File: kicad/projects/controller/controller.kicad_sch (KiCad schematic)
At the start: 30 parts, among them J1 Buttons, J2 Joystick1, J3 Joystick2, J4 Display, J5 18650, J6 Rumble1, J7 Rumble2, J8 ADS1115, Q1 DMG2301L, Q2 MMBT2222A, SW2 SW_DP3T, U2 ESP32-C6-SUPERMINI, U3 MCP1826T-3302E/DC

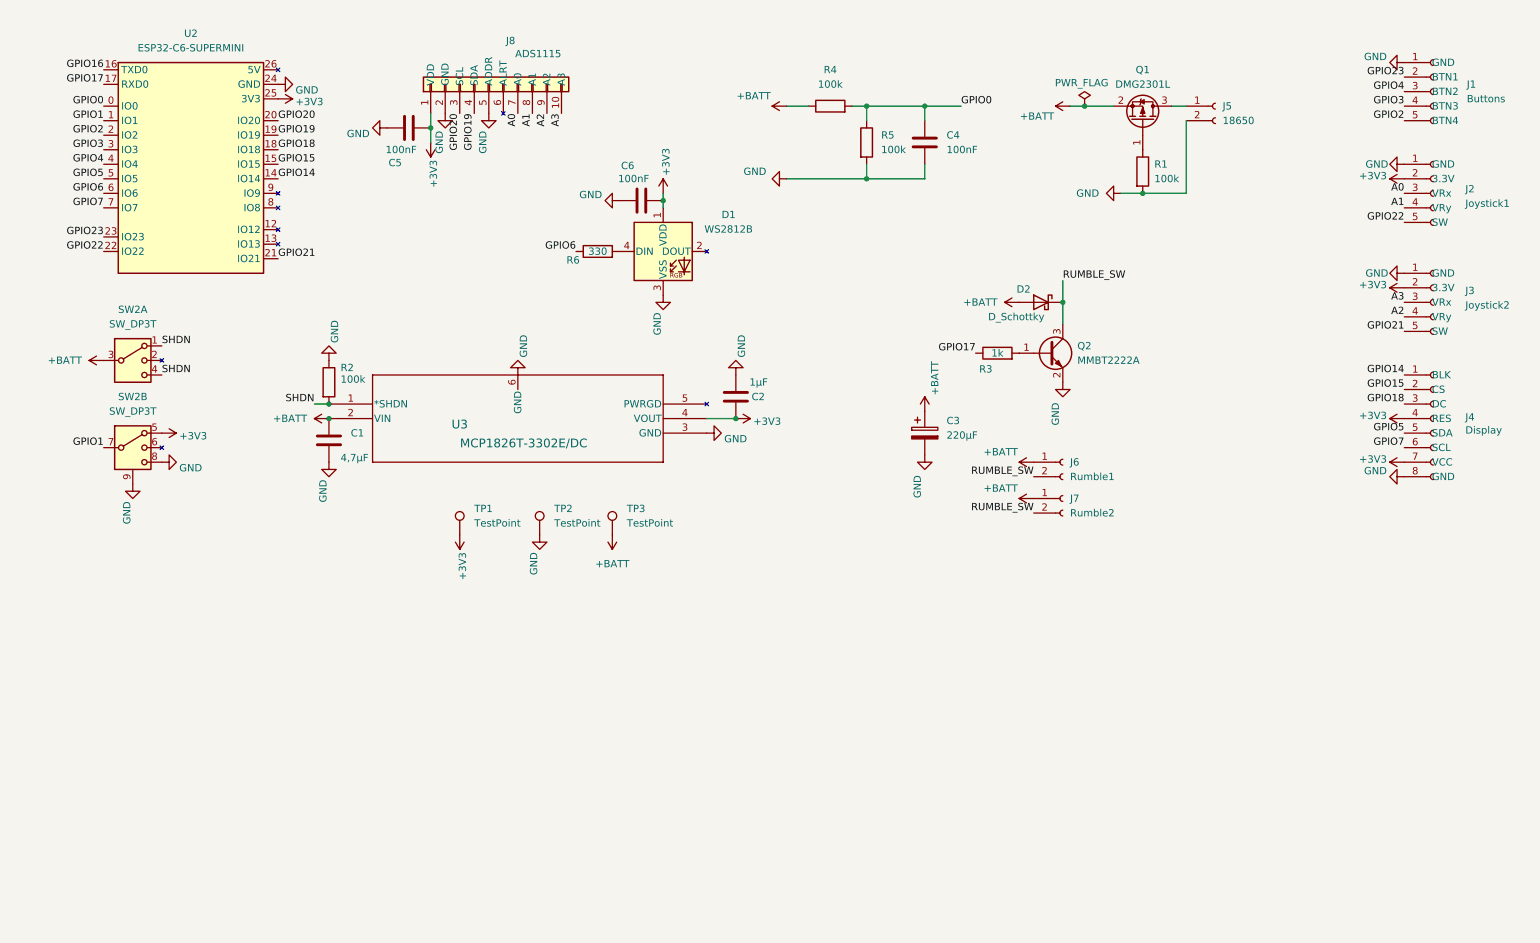
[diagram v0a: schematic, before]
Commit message: Repo für Veröffentlichung vorbereitet: KiCad-Struktur, Lizenz, Aufräumen
- KiCad-Projekte je Platine nach kicad/projects/<board>/ (kart, controller,
  buttons, switch), eigene Bibliotheken nach kicad/libs/, projektlokale
  sym-lib-table/fp-lib-table auf ${KIPRJMOD}/../../libs
- Schalter-Platinchen: einschalter -> switch, Titelblock vereinheitlicht
- AO4407A: 3D-Modell auf KiCad-Standard-SOIC-8, Footprint-Verweis korrigiert
- Alte Stände nach kicad/archive/ (FB-V1-Layout, D1-Mini-Schaltplan)
- Lizenz CC BY-NC-SA 4.0, Fan-Projekt-Hinweis
- CLAUDE.md nicht mehr versioniert, PDFs/DOCX/Exporte ignoriert
- Laufende Firmware-Änderungen (Kart V2, FB V2, Stern-Licht) mitcommittet
- docs/wiki-plan.md: Arbeitsliste für das Wiki

Co-Authored-By: Claude Opus 5.5 <noreply@anthropic.com>
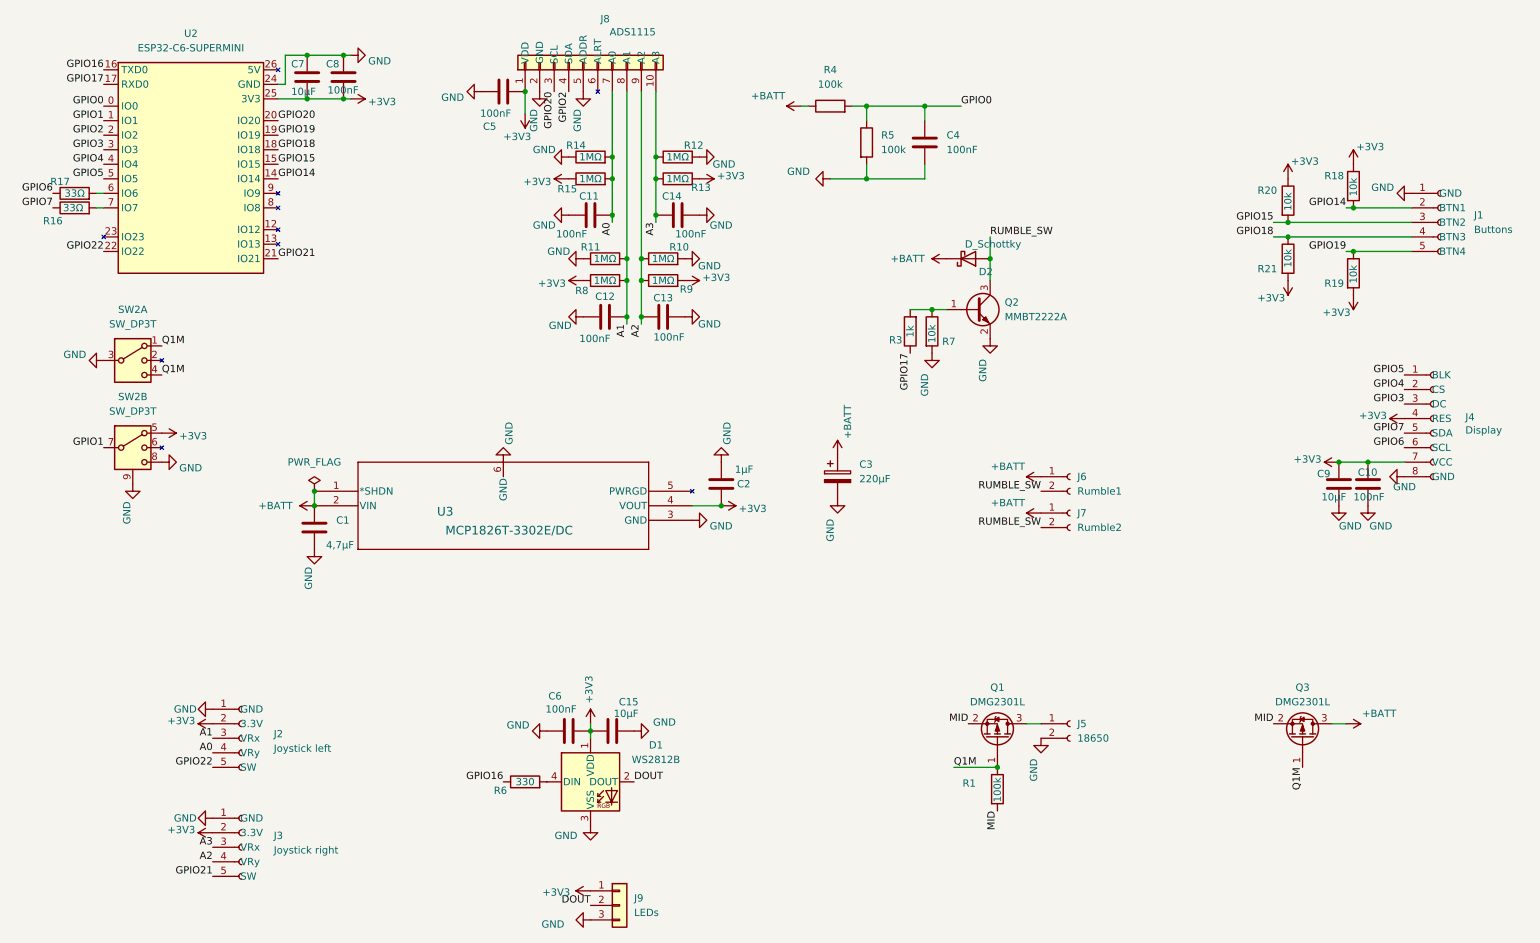
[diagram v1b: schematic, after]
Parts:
- removed R2: 100k, Resistor_SMD:R_0805_2012Metric_Pad1.20x1.40mm_HandSolder, symbol Device:R
- removed TP1, TP2, TP3: TestPoint, TestPoint:TestPoint_Pad_D2.0mm, symbol Connector:TestPoint
- added C10, C11, C12, C13, C14, C8: 100nF, Capacitor_SMD:C_0805_2012Metric_Pad1.18x1.45mm_HandSolder, symbol Device:C
- added C15, C7, C9: 10µF, Capacitor_SMD:C_1206_3216Metric_Pad1.33x1.80mm_HandSolder, symbol Device:C
- added J9: LEDs, Connector_PinHeader_2.54mm:PinHeader_1x03_P2.54mm_Vertical, symbol Connector_Generic:Conn_01x03
- added Q3: DMG2301L, Package_TO_SOT_SMD:SOT-23_Handsoldering, symbol Transistor_FET:DMG2301L
- added R10, R11, R12, R13, R14, R15, R8, R9: 1MΩ, Resistor_SMD:R_0805_2012Metric_Pad1.20x1.40mm_HandSolder, symbol Device:R
- added R16, R17: 33Ω, Resistor_SMD:R_0805_2012Metric_Pad1.20x1.40mm_HandSolder, symbol Device:R
- added R18, R19, R20, R21, R7: 10k, Resistor_SMD:R_0805_2012Metric_Pad1.20x1.40mm_HandSolder, symbol Device:R
- J1: footprint Connector_JST:JST_XH_S5B-XH-A-1_1x05_P2.50mm_Horizontal -> Connector_PinHeader_2.54mm:PinHeader_1x05_P2.54mm_Vertical
- J2: value Joystick1 -> Joystick left
- J3: value Joystick2 -> Joystick right
- J5: footprint Connector_Wire:SolderWire-1.5sqmm_1x02_P6mm_D1.7mm_OD3mm -> Connector_Wire:SolderWire-0.75sqmm_1x02_P4.8mm_D1.25mm_OD2.3mm
- J6, J7: footprint Connector_JST:JST_XH_S2B-XH-A-1_1x02_P2.50mm_Horizontal -> Connector_PinHeader_2.54mm:PinHeader_1x02_P2.54mm_Vertical
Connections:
- net +3V3: now also C10.1, C15.1, C7.2, C8.2, C9.1, J9.1 (Pin_1), R13.2, R15.1, R18.1, R19.2, R20.1, R21.2, R8.1, R9.2
- net +BATT: now also D2.1 (K), U3.1 (*SHDN), Q3.3 (D); no longer D2.2 (A), Q1.2 (S), SW2.3
- net A0: now also J2.4 (VRy), C11.2, R14.2, R15.2; no longer J2.3 (VRx)
- net A1: now also J2.3 (VRx), C12.1, R11.2, R8.2; no longer J2.4 (VRy)
- net A2: now also C13.1, R10.1, R9.1
- net A3: now also C14.1, R12.1, R13.1
- net GND: now also SW2.3, C10.2, C11.1, C12.2, C13.2, C14.2, C15.2, C7.1, C8.1, C9.2, J9.3 (Pin_3), R10.2, R11.1, R12.2, R14.1, R7.2; no longer R1.2
- net GPIO14: now also J1.2 (BTN1), R18.2; no longer J4.1 (BLK)
- net GPIO15: now also J1.3 (BTN2), R20.2; no longer J4.2 (CS)
- net GPIO16: now also R6.1
- net GPIO18: now also J1.4 (BTN3), R21.1; no longer J4.3 (DC)
- net GPIO19: now also J1.5 (BTN4), R19.1; no longer J8.4 (SDA)
- net GPIO2: now also J8.4 (SDA); no longer J1.5 (BTN4)
- net GPIO3: now also J4.3 (DC); no longer J1.4 (BTN3)
- net GPIO4: now also J4.2 (CS); no longer J1.3 (BTN2)
- net GPIO5: now also J4.1 (BLK); no longer J4.5 (SDA)
- net GPIO6: now also J4.6 (SCL), R17.1; no longer R6.1, U2.6 (IO6)
- net GPIO7: now also J4.5 (SDA), R16.1; no longer J4.6 (SCL), U2.7 (IO7)
- net RUMBLE_SW: now also D2.2 (A); no longer D2.1 (K)
- net Q1M: now reaches Q1.1 (G), R1.1
- net Q1M: now also SW2.1, SW2.4, Q3.1 (G)
- net at Q2.1 (B), R3.2: now also R7.1
- net DOUT: now reaches D1.2 (DOUT)
- net DOUT: now also J9.2 (Pin_2)
- net GPIO23: no longer names the net of U2.23 (IO23)
- net GPIO23: no longer J1.2 (BTN1)
- removed net SHDN: SW2.1, SW2.4, U3.1 (*SHDN)
- new net: R17.2, U2.6 (IO6)
- new net: R16.2, U2.7 (IO7)
- new net MID: Q1.2 (S), Q3.2 (S), R1.2
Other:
- moved on the sheet: C1, C2, C3, C5, C6, D2, J1, J2, J3, J6, J7, J8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
